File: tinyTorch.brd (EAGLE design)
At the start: 52.5 x 32 mm, 29 parts, among them Q1 FDG6303N, U1 MCP1640, U2 ATtiny84A-SSU

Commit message: v1 as sent to fab.
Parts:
- U1: value MCP1640 -> MCP1640D
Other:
- board text added: "open source goo.gl/xpB4pj"
- board text removed: "open source goo.gl/abcdefgh"
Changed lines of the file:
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@@
 <text x="36" y="2" size="1.4224" layer="21" ratio="16" align="center">UP/COLOR</text>
 <text x="28.5" y="16" size="1.016" layer="21" ratio="16" rot="SR270" align="bottom-center">open source
-goo.gl/abcdefgh</text>
+goo.gl/xpB4pj</text>
 <text x="2" y="29.5" size="1.27" layer="21" ratio="16">tinyTorch v1</text>
 <text x="2" y="27.5" size="1.016" layer="21" ratio="16">CC BY-SA 4.0 jc 0117</text>
@@
 <text x="38" y="16.5" size="1.27" layer="22" ratio="16" rot="MR90" align="bottom-center">CC BY-SA 4.0 jc 0117</text>
 <text x="26.5" y="16" size="1.4224" layer="22" ratio="16" rot="SMR90" align="bottom-center">open source
-goo.gl/abcdefgh</text>
+goo.gl/xpB4pj</text>
 </plain>
 <attributes>
@@
 <attribute name="VALUE" x="46.5" y="8" size="0.8128" layer="27" ratio="16" rot="R90"/>
 </element>
-<element name="U1" library="_jc" package="SOT23-6" value="MCP1640" x="8" y="13" smashed="yes" rot="R90">
+<element name="U1" library="_jc" package="SOT23-6" value="MCP1640D" x="8" y="13" smashed="yes" rot="R90">
 <attribute name="NAME" x="10.5" y="13" size="0.8128" layer="21" ratio="16" rot="SR270"/>
 </element>
@@
 <attribute name="NAME" x="48.375" y="15.8334" size="0.8128" layer="25" ratio="16"/>
 <attribute name="VALUE" x="47.1966" y="16.2996" size="1.016" layer="27" ratio="16" rot="R270"/>
+<attribute name="MFR" value="Lite-On" x="49" y="19.5" size="1.778" layer="27" rot="R270" display="off"/>
+<attribute name="MFR-PART-NO" value="LTL2H3EZ1K" x="49" y="19.5" size="1.778" layer="27" rot="R270" display="off"/>
 </element>
 <element name="D4" library="_jc" package="LED5MM-OVAL" value="Red" x="49" y="4.5" smashed="yes" rot="R270">
 <attribute name="NAME" x="48.375" y="0.8334" size="0.8128" layer="25" ratio="16"/>
 <attribute name="VALUE" x="47.1966" y="1.2996" size="1.016" layer="27" ratio="16" rot="R270"/>
+<attribute name="MFR" value="Lite-On" x="49" y="4.5" size="1.778" layer="27" rot="R270" display="off"/>
+<attribute name="MFR-PART-NO" value="LTL2H3EZ1K" x="49" y="4.5" size="1.778" layer="27" rot="R270" display="off"/>
 </element>
 <element name="R1" library="_jc" package="M0805" value="15" x="44" y="27" smashed="yes" rot="R90">
@@
 <attribute name="NAME" x="36" y="25" size="1.016" layer="25" ratio="16" rot="R180" align="center"/>
 <attribute name="VALUE" x="36.508" y="28.81" size="1.016" layer="27" ratio="16" rot="R180" align="center"/>
+<attribute name="MFR" value="Omron" x="36" y="25" size="1.778" layer="27" rot="R180" display="off"/>
+<attribute name="MFR-PART-NO" value="B3FS-1000" x="36" y="25" size="1.778" layer="27" rot="R180" display="off"/>
 </element>
 <element name="S2" library="_jc" package="TACT-SW-SMT" value="UP/COLOR" x="36" y="7" smashed="yes">
 <attribute name="NAME" x="36" y="7" size="1.016" layer="25" ratio="16" align="center"/>
 <attribute name="VALUE" x="35.492" y="3.19" size="1.016" layer="27" ratio="16" align="center"/>
+<attribute name="MFR" value="Omron" x="36" y="7" size="1.778" layer="27" display="off"/>
+<attribute name="MFR-PART-NO" value="B3FS-1000" x="36" y="7" size="1.778" layer="27" display="off"/>
 </element>
 <element name="LOGO1" library="ohw-logo" package="OSHW_8X150_NOTEXT" value="OSHW_LOGO_8MILX0150-NT" x="31.5" y="18" smashed="yes" rot="R270"/>
@@
 <contactref element="D2" pad="K"/>
 <contactref element="R2" pad="2"/>
-<wire x1="46" y1="17" x2="44.5" y2="18.5" width="0.3048" layer="16"/>
 <via x="44.5" y="18.5" extent="1-16" drill="0.6"/>
 <wire x1="44.5" y1="18.5" x2="44.5" y2="20.05" width="0.3048" layer="1"/>
 <wire x1="44.5" y1="20.05" x2="44" y2="20.55" width="0.3048" layer="1"/>
-<wire x1="46" y1="17" x2="46" y2="11.7" width="0.3048" layer="16"/>
-<wire x1="46" y1="11.7" x2="47" y2="10.7" width="0.3048" layer="16"/>
-<wire x1="47" y1="10.7" x2="48.97" y2="10.7" width="0.3048" layer="16"/>
+<wire x1="46.8" y1="10.7" x2="44.5" y2="13" width="0.3048" layer="16"/>
+<wire x1="44.5" y1="13" x2="44.5" y2="18.5" width="0.3048" layer="16"/>
+<wire x1="46.8" y1="10.7" x2="48.97" y2="10.7" width="0.3048" layer="16"/>
 <wire x1="48.97" y1="10.7" x2="49" y2="10.73" width="0.3048" layer="16"/>
 </signal>

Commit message: Tweak resistor values.
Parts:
- R3, R4: value 65 -> 62
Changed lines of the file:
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@@
 <attribute name="VALUE" x="41.5" y="23" size="0.8128" layer="27" ratio="16" rot="R270"/>
 </element>
-<element name="R3" library="_jc" package="M0805" value="65" x="44" y="9.5" smashed="yes" rot="R90">
+<element name="R3" library="_jc" package="M0805" value="62" x="44" y="9.5" smashed="yes" rot="R90">
 <attribute name="NAME" x="45.6" y="9.2" size="0.8128" layer="25" ratio="16" rot="SR270"/>
 <attribute name="VALUE" x="46.5" y="8" size="0.8128" layer="27" ratio="16" rot="R90"/>
@@
 <attribute name="VALUE" x="46.5" y="25.5" size="0.8128" layer="27" ratio="16" rot="R90"/>
 </element>
-<element name="R4" library="_jc" package="M0805" value="65" x="44" y="4" smashed="yes" rot="R270">
+<element name="R4" library="_jc" package="M0805" value="62" x="44" y="4" smashed="yes" rot="R270">
 <attribute name="NAME" x="41.7" y="5.8" size="0.8128" layer="25" ratio="16" rot="SR270"/>
 <attribute name="VALUE" x="41.5" y="5.5" size="0.8128" layer="27" ratio="16" rot="R270"/>

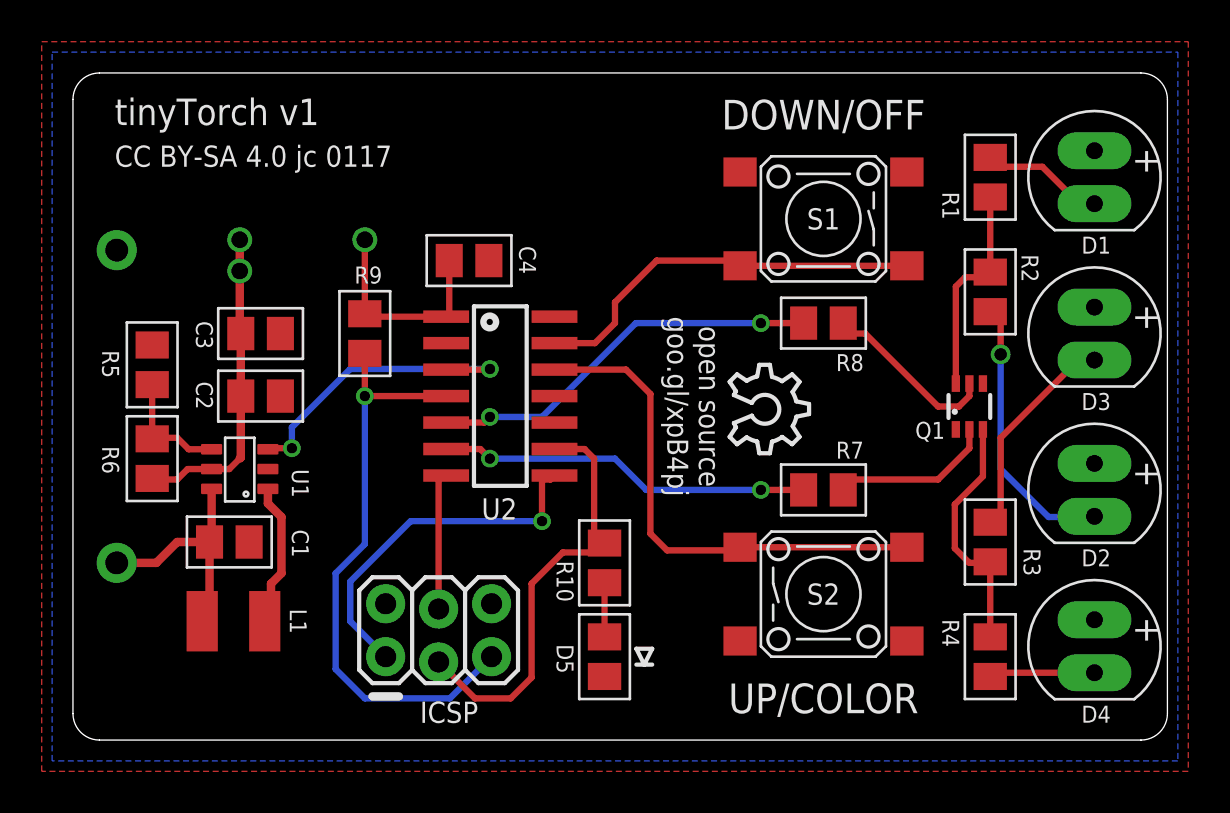
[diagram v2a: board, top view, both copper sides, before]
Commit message: Minor board layout tweaks.
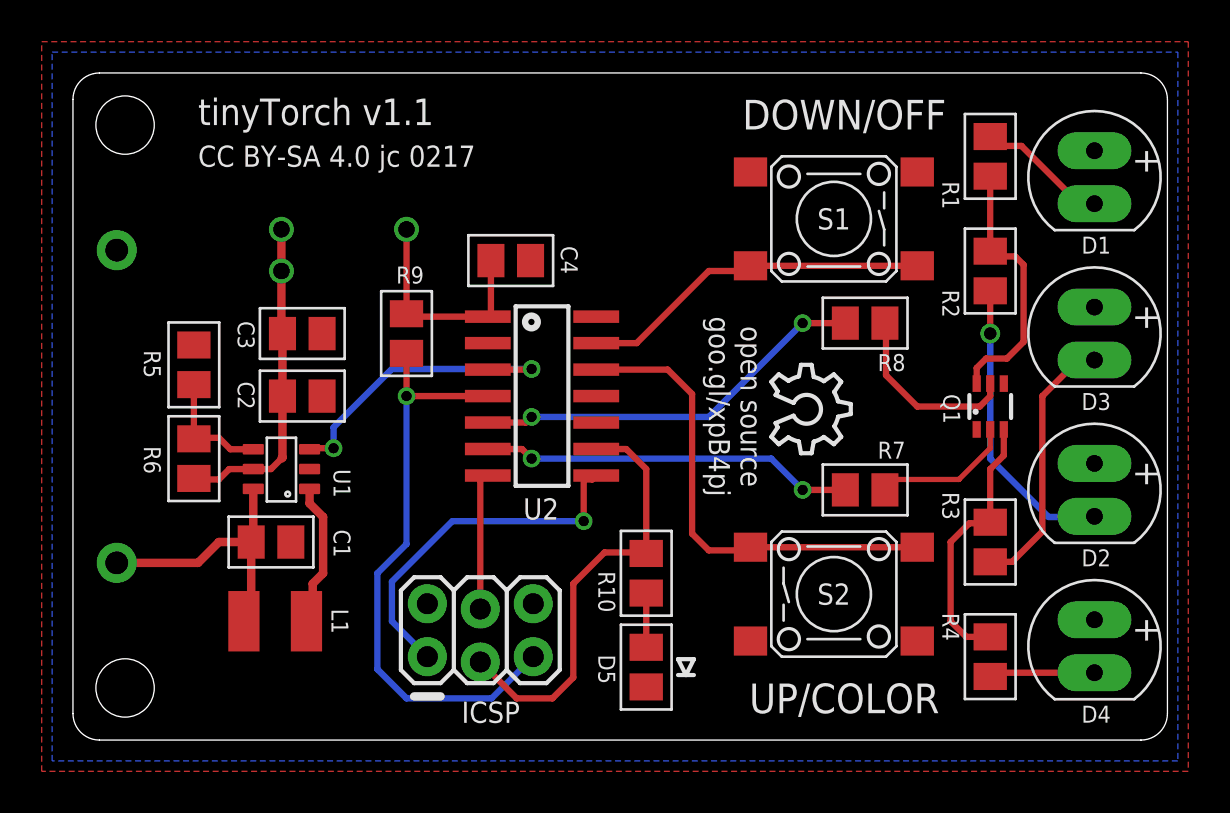
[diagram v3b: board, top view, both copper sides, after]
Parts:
- moved D5 2.06 mm to (27.5, 3.50)
- moved R10 2.06 mm to (27.5, 8.00)
- moved C1 2.00 mm to (9.50, 9.50)
- moved C2 2.00 mm to (11.0, 16.5)
- moved C3 2.00 mm to (11.0, 19.5)
- moved C4 2.00 mm to (21.0, 23.0)
- moved ICSP 2.00 mm to (17.0, 4.00)
- moved LOGO1 2.00 mm to (33.5, 18.0)
- moved R5 2.00 mm to (5.80, 18.0)
- moved R6 2.00 mm to (5.80, 13.5)
- moved R7 2.00 mm to (38.0, 12.0)
- moved R8 2.00 mm to (38.0, 20.0)
- moved R9 2.00 mm to (16.0, 19.5)
- moved U1 2.00 mm to (10.0, 13.0)
- moved U2 2.00 mm to (22.5, 16.5)
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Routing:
- net N$10: track 10.3 -> 12.8 mm
- net N$13: track 10.2 -> 12.7 mm
- net N$15: track 19.2 -> 16.9 mm
- net N$11: track 11.6 -> 13.6 mm
- net N$16: track 24.5 -> 22.9 mm
- net N$14: track 11.9 -> 13.0 mm
- net VCC: track 25.4 -> 26.4 mm
- net N$9: track 13.2 -> 14.2 mm
- net N$1: track 7.78 -> 6.78 mm
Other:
- board text added: "CC BY-SA 4.0 jc 0217"
- board text added: "tinyTorch v1.1"
- board text removed: "CC BY-SA 4.0 jc 0117"
- board text removed: "tinyTorch v1"
